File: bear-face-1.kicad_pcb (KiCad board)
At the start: 2 copper layers, 301.7 x 112.6 mm, 190 parts, among them SW1 SW_Push, U1 ATmega32U4-AU, Y1 16MHz

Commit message: Row tracks drawn
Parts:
- moved F1 5.72 mm to (87.8, 77.9)
- moved R3 5.72 mm to (85.3, 77.9)
- moved R2 5.72 mm to (82.9, 77.9)
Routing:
- net ROW5: track 0.00 -> 278.3 mm
- net ROW3: track 15.2 -> 278.6 mm
- net ROW2: track 17.8 -> 280.9 mm
- net ROW0: track 17.8 -> 273.4 mm
- net ROW1: track 17.8 -> 269.2 mm
- net ROW4: track 5.08 -> 240.3 mm
- net Net-(USB1-Pad6): track 0.00 -> 13.9 mm
- net D-: track 0.00 -> 4.08 mm
- net D+: track 0.00 -> 4.07 mm
- net Net-(R3-Pad1): track 0.00 -> 0.97 mm
- net Net-(R2-Pad1): track 0.00 -> 0.97 mm

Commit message: Columns drawn in
Ignore differential pair - going to take some work
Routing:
- net Net-(R2-Pad1): track 0.97 -> 141.4 mm
- net Net-(R3-Pad1): track 0.97 -> 140.9 mm, vias 0 -> 2
- net COL9: track 0.00 -> 111.0 mm
- net COL10: track 0.00 -> 111.0 mm
- net COL5: track 0.00 -> 110.0 mm
- net COL12: track 0.00 -> 107.1 mm
- net COL11: track 0.00 -> 107.1 mm
- net COL0: track 0.00 -> 106.1 mm
- net COL13: track 0.00 -> 105.1 mm
- net COL14: track 0.00 -> 97.2 mm
- net COL1: track 0.00 -> 93.9 mm
- net COL2: track 0.00 -> 91.0 mm
- net COL8: track 0.00 -> 90.0 mm
- net COL7: track 0.00 -> 90.0 mm
- net COL6: track 0.00 -> 90.0 mm
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
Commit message: Fixed dPair, USB connector schematic
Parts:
- removed USB1: Molex-0548190589, Connector_USB:USB_Micro-B_GCT_USB3076-30-A
- added J1: USB_B_Micro, Connector_USB:USB_Micro-B_Wuerth_629105150521, B.Cu at (83.8, 72.1)
- moved R3 2.92 mm to (82.4, 77.9)
- moved R2 1.65 mm to (84.6, 77.9)
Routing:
- net Net-(USB1-Pad6): track 13.9 -> 0.00 mm
- net Net-(R3-Pad1): track 140.9 -> 139.7 mm, vias 2 -> 0
- net Net-(R2-Pad1): track 141.4 -> 140.2 mm
- net D-: track 4.08 -> 3.24 mm
- net D+: track 4.07 -> 3.24 mm

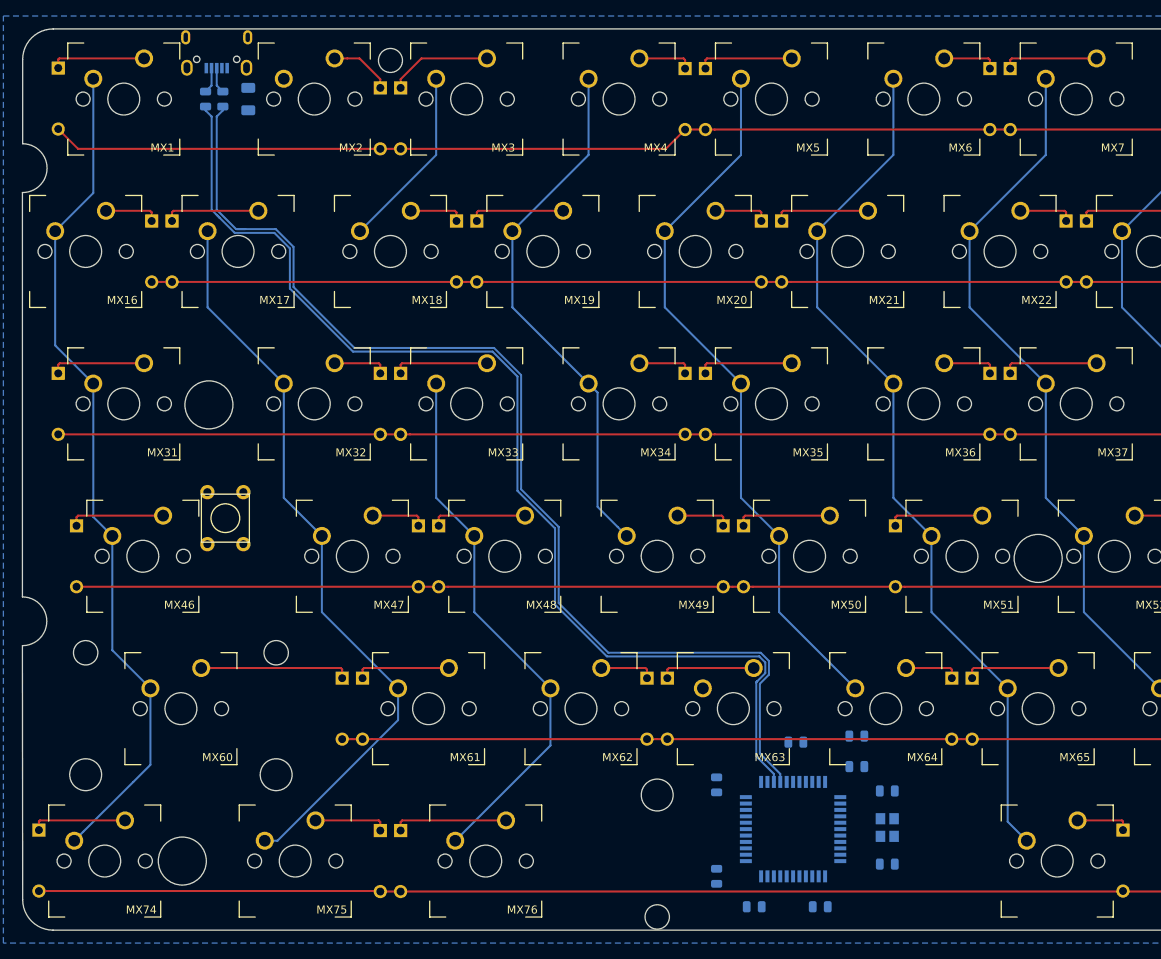
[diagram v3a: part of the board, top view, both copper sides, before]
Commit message: Tracks nearly complete
All tracks except for MCU, USB
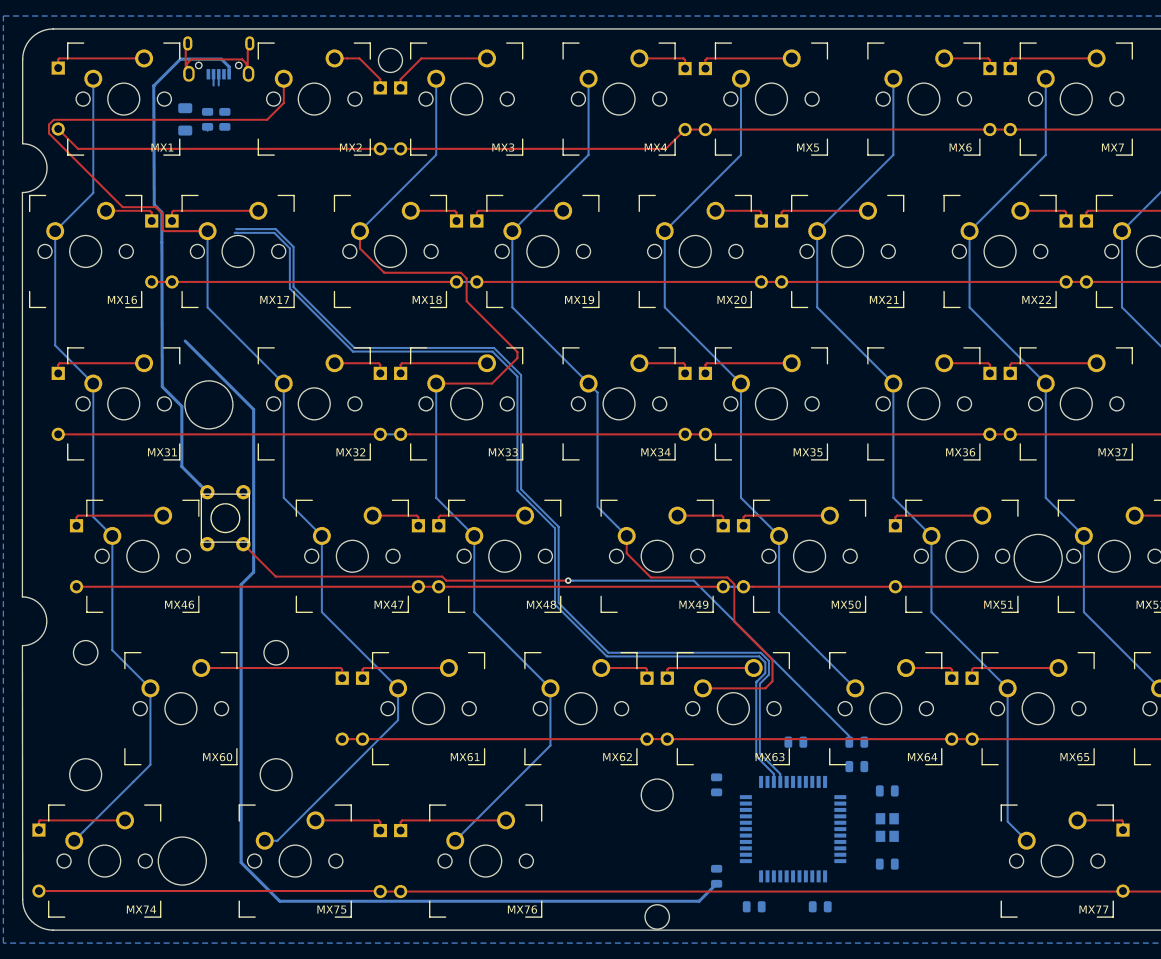
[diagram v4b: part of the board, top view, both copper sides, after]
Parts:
- moved F1 8.27 mm to (79.9, 80.4)
- moved R2 2.55 mm to (84.8, 80.4)
- moved R3 2.55 mm to (82.7, 80.4)
- moved J1 0.80 mm to (84.1, 72.8)
- moved R1 0.76 mm to (163.8, 158.2)
- turned SW1 to 90 degrees
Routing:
- net +5V: track 0.00 -> 131.7 mm
- net Net-(R1-Pad2): track 0.00 -> 86.4 mm, vias 0 -> 1
- net GND: track 0.00 -> 65.7 mm
- net COL1: track 93.9 -> 154.5 mm
- net COL2: track 91.0 -> 132.4 mm
- net COL3: track 67.0 -> 107.4 mm
- net Net-(J1-Pad6): track 0.00 -> 18.6 mm
- net Net-(R3-Pad1): track 139.7 -> 122.7 mm
- net Net-(R2-Pad1): track 140.2 -> 123.5 mm
- net D+: track 3.24 -> 1.40 mm
- net D-: track 3.24 -> 1.42 mm

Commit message: Track tweaks
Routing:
- net VCC: track 0.00 -> 5.95 mm
- net D+: track 1.40 -> 6.43 mm
- net D-: track 1.42 -> 6.44 mm
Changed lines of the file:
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@@
     (thickness 1.6)
     (drawings 14)
-    (tracks 612)
+    (tracks 619)
     (zones 0)
     (modules 190)
@@
   (segment (start 349.377 170.561) (end 349.377 151.511) (width 0.254) (layer B.Cu) (net 105))
   (segment (start 84.074 76.1515) (end 84.074 74.7472) (width 0.254) (layer B.Cu) (net 106))
+  (segment (start 84.074 78.6915) (end 84.836 79.4535) (width 0.254) (layer B.Cu) (net 106))
+  (segment (start 84.074 74.7472) (end 84.074 78.6915) (width 0.254) (layer B.Cu) (net 106))
   (segment (start 83.424 76.1665) (end 83.424 74.7472) (width 0.254) (layer B.Cu) (net 107))
+  (segment (start 83.424 78.7065) (end 83.424 74.7472) (width 0.254) (layer B.Cu) (net 107))
+  (segment (start 82.677 79.4535) (end 83.424 78.7065) (width 0.254) (layer B.Cu) (net 107))
+  (segment (start 80.758 78.991) (end 79.883 78.991) (width 0.381) (layer B.Cu) (net 108))
+  (segment (start 82.774 76.975) (end 80.758 78.991) (width 0.381) (layer B.Cu) (net 108))
+  (segment (start 82.774 74.7472) (end 82.774 76.975) (width 0.381) (layer B.Cu) (net 108))
   (segment (start 88.440001 116.656059) (end 88.440001 136.984999) (width 0.381) (layer B.Cu) (net 112))
   (segment (start 79.883 108.099058) (end 88.440001 116.656059) (width 0.381) (layer B.Cu) (net 112))

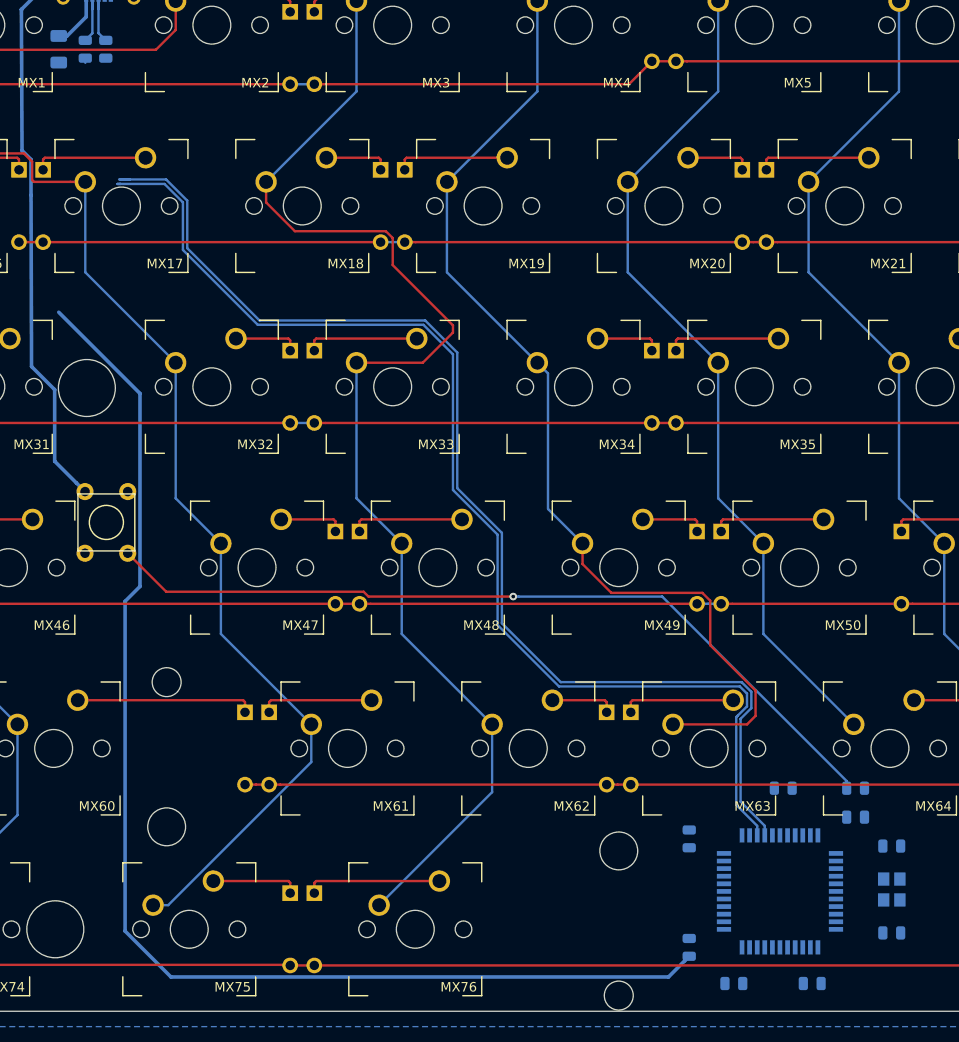
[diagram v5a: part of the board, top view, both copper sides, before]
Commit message: MCU tracks done
All tracks done except for switch matrix
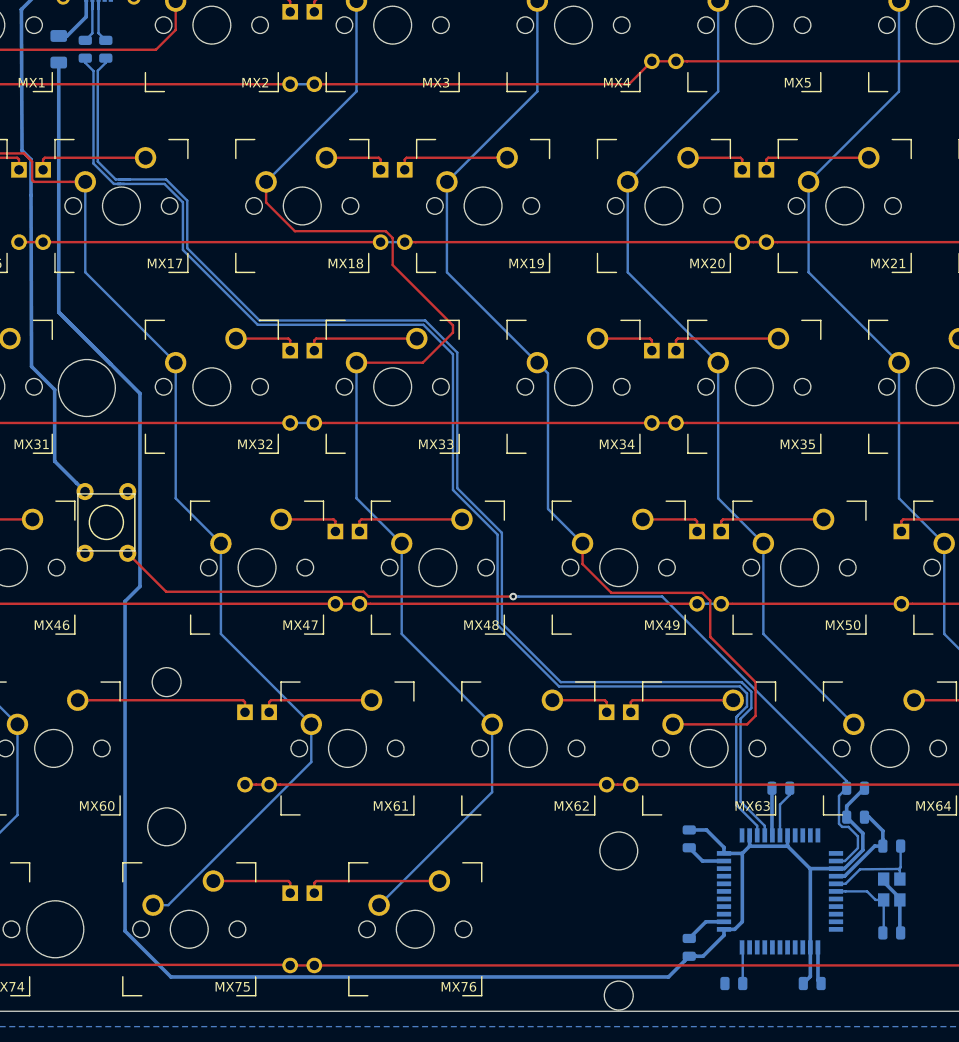
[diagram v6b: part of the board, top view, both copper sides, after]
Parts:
- moved C1 9.14 mm to (167.6, 173.5), turned to 0 degrees
- moved C2 9.14 mm to (167.6, 164.3), turned to 180 degrees
- moved C3 0.25 mm to (156.0, 158.2)
- turned C5 to 0 degrees
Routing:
- net +5V: track 131.7 -> 225.0 mm
- net GND: track 65.7 -> 100.2 mm
- net Net-(R3-Pad1): track 122.7 -> 137.8 mm
- net Net-(R2-Pad1): track 123.5 -> 138.4 mm
- net Net-(C2-Pad1): track 0.00 -> 11.0 mm
- net Net-(R1-Pad2): track 86.4 -> 97.2 mm
- net Net-(C1-Pad1): track 0.00 -> 8.91 mm
- net Net-(C3-Pad1): track 0.00 -> 5.39 mm
- net Net-(R4-Pad2): track 0.00 -> 3.84 mm

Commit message: MCU tracks complete
5V no longer running under MCU, all GNDs and 5V nets tied in.
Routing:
- net GND: track 100.2 -> 150.9 mm
- net +5V: track 225.0 -> 263.1 mm, vias 0 -> 3

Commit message: Tracks finished, DRC check passed
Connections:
- U1 pad 1: Net-(U1-Pad1) -> ROW1
- U1 pad 10: Net-(U1-Pad10) -> COL4
- U1 pad 11: Net-(U1-Pad11) -> ROW3
- U1 pad 12: Net-(U1-Pad12) -> COL5
- U1 pad 18: Net-(U1-Pad18) -> COL6
- U1 pad 19: Net-(U1-Pad19) -> COL7
- U1 pad 20: Net-(U1-Pad20) -> COL8
- U1 pad 21: Net-(U1-Pad21) -> COL9
- U1 pad 22: Net-(U1-Pad22) -> COL10
- U1 pad 25: Net-(U1-Pad25) -> COL11
- U1 pad 26: Net-(U1-Pad26) -> COL12
- U1 pad 27: Net-(U1-Pad27) -> COL13
- U1 pad 28: Net-(U1-Pad28) -> COL14
- U1 pad 36: Net-(U1-Pad36) -> ROW5
- U1 pad 37: Net-(U1-Pad37) -> COL1
- U1 pad 38: Net-(U1-Pad38) -> COL2
- U1 pad 39: Net-(U1-Pad39) -> COL0
- U1 pad 40: Net-(U1-Pad40) -> ROW4
- U1 pad 41: Net-(U1-Pad41) -> COL3
- U1 pad 8: Net-(U1-Pad8) -> ROW2
- U1 pad 9: Net-(U1-Pad9) -> ROW0
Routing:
- net COL14: track 97.2 -> 314.8 mm
- net COL13: track 105.1 -> 294.7 mm
- net COL12: track 107.1 -> 275.1 mm
- net COL11: track 107.1 -> 262.8 mm
- net GND: track 150.9 -> 278.9 mm, vias 0 -> 1
- net COL10: track 111.0 -> 229.7 mm
- net COL9: track 111.0 -> 221.0 mm
- net ROW0: track 273.4 -> 372.4 mm
- net COL8: track 90.0 -> 180.8 mm
- net COL0: track 106.1 -> 192.8 mm, vias 0 -> 1
- net ROW1: track 269.2 -> 355.8 mm, vias 0 -> 2
- net COL7: track 90.0 -> 161.8 mm
- net COL1: track 154.5 -> 219.9 mm
- net COL6: track 90.0 -> 152.0 mm
- net ROW5: track 278.3 -> 340.1 mm
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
